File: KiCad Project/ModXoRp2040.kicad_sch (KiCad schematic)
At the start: 0 parts

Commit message: start pcb layout
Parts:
- added J1: LPC, symbol Connector_Generic:Conn_02x08_Odd_Even
- added R1, R2: 100, symbol Device:R_Small
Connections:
- new net: J1.15 (Pin_15), R2.2
- new net: J1.9 (Pin_9), R1.2
- new net 3.3v: R1.1, R2.1
- new net 5v: J1.6 (Pin_6)
- new net GND: J1.12 (Pin_12), J1.2 (Pin_2)
- new net RST: J1.5 (Pin_5)
- no-connect marks 0 -> 2

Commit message: finish schematics, start on pcb layout
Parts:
- added C1, C10, C11, C12, C13, C14, C17, C18, C2, C20, C4, C6, C7, C8, C9: 100nF, Capacitor_SMD:C_0402_1005Metric, symbol Device:C
- added C15, C16: 10uF, Capacitor_SMD:C_0805_2012Metric, symbol Device:C
- added C19, C3, C5: 1uF, Capacitor_SMD:C_0402_1005Metric, symbol Device:C
- added CXTAL1, CXTAL2: 30pF, Capacitor_SMD:C_0402_1005Metric, symbol Device:C_Small
- added D1: D_Schottky, Diode_SMD:D_SMA, symbol Device:D_Schottky
- added D3: WS2812B, LED_SMD:LED_WS2812B_PLCC4_5.0x5.0mm_P3.2mm, symbol LED:WS2812B
- added D4: STM_LED2, LED_SMD:LED_0402_1005Metric_Pad0.77x0.64mm_HandSolder, symbol Device:LED
- added D5: SS34, Diode_SMD:D_SMA, symbol Device:D_Schottky
- added FU1: 0.5A, Fuse:Fuse_1206_3216Metric_Pad1.42x1.75mm_HandSolder, symbol Device:Fuse
- added J10: STM EN SCL, Jumper:SolderJumper-2_P1.3mm_Open_RoundedPad1.0x1.5mm, symbol Connector_Generic:Conn_01x02
- added J11: USB_C_Receptacle_USB2.0, Connector_USB:USB_C_Receptacle_G-Switch_GT-USB-7010ASV, symbol Connector:USB_C_Receptacle_USB2.0
- added J12: Conn_01x05, Connector_PinSocket_2.54mm:PinSocket_1x05_P2.54mm_Vertical, symbol Connector_Generic:Conn_01x05
- added J13: Display Exp, Connector_JST:JST_SH_SM06B-SRSS-TB_1x06-1MP_P1.00mm_Horizontal, symbol Connector_Generic:Conn_01x06
- added J2: PROG SM32, Connector_PinSocket_2.54mm:PinSocket_1x08_P2.54mm_Vertical, symbol Connector_Generic:Conn_01x08
- added J3: STM EN, Jumper:SolderJumper-2_P1.3mm_Open_RoundedPad1.0x1.5mm, symbol Connector_Generic:Conn_01x02
- added J4: RGB Exp, Connector_JST:JST_SH_SM06B-SRSS-TB_1x06-1MP_P1.00mm_Horizontal, symbol Connector_Generic:Conn_01x06
- added J5: I2C Exp, Connector_JST:JST_SH_SM06B-SRSS-TB_1x06-1MP_P1.00mm_Horizontal, symbol Connector_Generic:Conn_01x06
- added J6: STM Dbg, Connector_JST:JST_SH_SM06B-SRSS-TB_1x06-1MP_P1.00mm_Horizontal, symbol Connector_Generic:Conn_01x06
- added J8: D0, TestPoint:TestPoint_Pad_D1.5mm, symbol Connector_Generic:Conn_01x01
- added J9: STM EN SDA, Jumper:SolderJumper-2_P1.3mm_Open_RoundedPad1.0x1.5mm, symbol Connector_Generic:Conn_01x02
- added R10, RRST1: 10K, Resistor_SMD:R_0603_1608Metric_Pad0.98x0.95mm_HandSolder, symbol Device:R
- added R11, R9: 1K, Resistor_SMD:R_0402_1005Metric_Pad0.72x0.64mm_HandSolder, symbol Device:R
- added R12, R6: 5.1k, Resistor_SMD:R_0603_1608Metric_Pad0.98x0.95mm_HandSolder, symbol Device:R
- added R13, R14, R15, R5: 2k, Resistor_SMD:R_0402_1005Metric_Pad0.72x0.64mm_HandSolder, symbol Device:R_Small
- added R16: 1K, Resistor_SMD:R_0603_1608Metric_Pad0.98x0.95mm_HandSolder, symbol Device:R
- added R3, R4: 100, Resistor_SMD:R_0402_1005Metric_Pad0.72x0.64mm_HandSolder, symbol Device:R_Small
- added R7, R8: 27, Resistor_SMD:R_0402_1005Metric_Pad0.72x0.64mm_HandSolder, symbol Device:R
- added SWBOOT1, SWRST1: K2-1187SQ-C4SW-06, Jumper:SolderJumper-2_P1.3mm_Open_RoundedPad1.0x1.5mm, symbol Switch:SW_Push
- added U1: RP2040, Package_DFN_QFN:QFN-56-1EP_7x7mm_P0.4mm_EP3.2x3.2mm, symbol MCU_RaspberryPi_RP2040:RP2040
- added U2: USBLC6-2P6, Package_TO_SOT_SMD:SOT-666, symbol Power_Protection:USBLC6-2P6
- added U3: STM32F030C8Tx, Package_QFP:LQFP-48_7x7mm_P0.5mm, symbol MCU_ST_STM32F0:STM32F030C8Tx
- added UF1: W25Q128JVS, libs:SOIC-8_5.275x5.275mm_P1.27mm, symbol Memory_Flash:W25Q128JVS
- added UV1: NCP1117-3.3_SOT223, Package_TO_SOT_SMD:SOT-223-3_TabPin2, symbol Regulator_Linear:NCP1117-3.3_SOT223
- added Y1: 12MHz, Crystal:Crystal_SMD_3225-4Pin_3.2x2.5mm, symbol Device:Crystal_GND24
- J1: footprint (none) -> Connector_PinSocket_2.54mm:PinSocket_2x08_P2.54mm_Vertical
- R1, R2: footprint (none) -> Resistor_SMD:R_0402_1005Metric_Pad0.72x0.64mm_HandSolder
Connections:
- net GND: now also C1.2, C10.2, C11.2, C12.1, C13.2, C14.2, C15.2, C16.2, C17.2, C18.2, C19.2, C2.2, C20.2, C3.2, C4.2, C5.2, C6.2, C7.2, C8.2, C9.2, CXTAL1.1, CXTAL2.1, D3.3 (VSS), J11.A1 (GND), J11.A12 (GND), J11.B1 (GND), J11.B12 (GND), J11.S1 (SHIELD), J12.1 (Pin_1), J2.7 (Pin_7), J4.3 (Pin_3), J4.4 (Pin_4), J4.5 (Pin_5), J5.1 (Pin_1), J6.1 (Pin_1), R12.1, R14.2, R16.1, R6.1, SWBOOT1.1, SWRST1.2, U1.19 (TESTEN), U1.57 (GND), U2.2 (GND), U3.23 (VSS), U3.8 (VSSA), UF1.4 (GND), UV1.1 (GND), Y1.2, Y1.4
- net RST: now also U1.9 (GPIO7)
- net LCLK: now reaches J1.1 (Pin_1)
- net LCLK: now also U1.6 (GPIO4)
- net at J1.10 (Pin_10): now also R3.2
- net at J1.11 (Pin_11): now also R2.2
- net XSCL: now reaches J1.13 (Pin_13)
- net XSCL: now also J10.2 (Pin_2), J5.2 (Pin_2)
- net XSDA: now reaches J1.14 (Pin_14)
- net XSDA: now also J5.5 (Pin_5), J9.2 (Pin_2)
- net 3.3v_xb: now reaches J1.15 (Pin_15)
- net 3.3v_xb: now also J1.9 (Pin_9), J4.2 (Pin_2), U1.11 (GPIO8); no longer R2.2
- net LFRAME: now reaches J1.3 (Pin_3)
- net LFRAME: now also U1.7 (GPIO5)
- net at J1.7 (Pin_7): now also R1.2
- net at J1.8 (Pin_8): now also R4.2
- net 3.3v renamed LAD0
- net LAD0: now also U1.2 (GPIO0); no longer R1.1
- net 5v: no longer names the net of J1.6 (Pin_6)
- net 5v: now also D1.2 (A)
- new net: CXTAL2.2, R11.2, Y1.3
- new net: J11.B5 (CC2), R12.2
- new net: J11.A6 (D+), J11.B6 (D+), U2.1 (I/O1)
- new net: J11.A7 (D-), J11.B7 (D-), U2.3 (I/O2)
- new net: FU1.2, J11.A4 (VBUS), J11.A9 (VBUS), J11.B4 (VBUS), J11.B9 (VBUS)
- new net: J11.A5 (CC1), R6.2
- new net: D4.1 (K), R16.2
- new net: D5.2 (A), FU1.1
- new net: R14.1, U3.44 (BOOT0)
- new net +1V1: C1.1, C2.1, C3.1, U1.23 (DVDD), U1.45 (VREG_VOUT), U1.50 (DVDD)
- new net +3V3: C10.1, C11.1, C13.1, C14.1, C16.1, C4.1, C5.1, C6.1, C7.1, C8.1, C9.1, J2.8 (Pin_8), J3.2 (Pin_2), R10.1, R13.1, R15.1, R5.2, RRST1.2, U1.1 (IOVDD), U1.10 (IOVDD), U1.22 (IOVDD), U1.33 (IOVDD), U1.42 (IOVDD), U1.43 (ADC_AVDD), U1.44 (VREG_IN), U1.48 (USB_VDD), U1.49 (IOVDD), UF1.8 (VCC), UV1.2 (VO)
- new net +5V: C15.1, C20.1, D1.1 (K), D3.1 (VDD), D5.1 (K), J13.1 (Pin_1), J4.6 (Pin_6), J5.6 (Pin_6), UV1.3 (VI)
- new net 5V: C12.2, U2.5 (VBUS)
- new net D0: J8.1 (Pin_1), U1.8 (GPIO6)
- new net DISP_CSN1: J13.5 (Pin_5), U1.39 (GPIO27_ADC1)
- new net DISP_CSN2: J13.4 (Pin_4), U1.38 (GPIO26_ADC0)
- new net DISP_SPI_SCK: J13.3 (Pin_3), U1.29 (GPIO18)
- new net DISP_SPI_TX: J13.2 (Pin_2), U1.30 (GPIO19)
- new net EX_SCL: J5.4 (Pin_4), U1.32 (GPIO21)
- new net EX_SDA: J5.3 (Pin_3), U1.31 (GPIO20)
- new net LAD1: R3.1, U1.3 (GPIO1)
- new net LAD2: R4.1, U1.4 (GPIO2)
- new net LAD3: R1.1, U1.5 (GPIO3)
- new net QSPI_SCLK: U1.52 (QSPI_SCLK), UF1.6 (CLK)
- new net QSPI_SD0: U1.53 (QSPI_SD0), UF1.5 (DI(IO0))
- new net QSPI_SD1: U1.55 (QSPI_SD1), UF1.2 (DO(IO1))
- new net QSPI_SD2: U1.54 (QSPI_SD2), UF1.3 (IO2)
- new net QSPI_SD3: U1.51 (QSPI_SD3), UF1.7 (IO3)
- new net QSPI_SS: R10.2, R9.1, U1.56 (QSPI_SS), UF1.1 (~{CS})
- new net RGB: D3.2 (DOUT), J4.1 (Pin_1)
- new net RP2040_RGB: D3.4 (DIN), U1.34 (GPIO22)
- new net RUN: RRST1.1, SWRST1.1, U1.26 (RUN)
- new net STM_3.3v: C17.1, C18.1, C19.1, J3.1 (Pin_1), U3.1 (VDD), U3.24 (VDD), U3.48 (VDD), U3.9 (VDDA)
- new net STM_INT: J6.6 (Pin_6), U3.36 (PF7)
- new net STM_LED: J6.2 (Pin_2), U3.2 (PC13)
- new net STM_LED2: D4.2 (A), U3.3 (PC14)
- new net STM_NRST: J2.3 (Pin_3), R15.2, U3.7 (NRST)
- new net STM_OSC: J2.4 (Pin_4), U3.6 (PF1)
- new net STM_RX: J2.6 (Pin_6), U3.13 (PA3)
- new net STM_SCL: J6.3 (Pin_3), J6.4 (Pin_4), R5.1, U3.42 (PB6)
- new net STM_SDA: J6.5 (Pin_5), R13.2, U3.43 (PB7)
- new net STM_SWCLK: J2.1 (Pin_1), U3.37 (PA14)
- new net STM_SWDIO: J2.2 (Pin_2), U3.34 (PA13)
- new net STM_TX: J2.5 (Pin_5), U3.12 (PA2)
- new net STM_XSCL: J10.1 (Pin_1), U3.21 (PB10)
- new net STM_XSDA: J9.1 (Pin_1), U3.22 (PB11)
- new net SWCLK: J12.3 (Pin_3), U1.24 (SWCLK)
- new net SWDIO: J12.2 (Pin_2), U1.25 (SWD)
- new net UART_RX: J12.4 (Pin_4), U1.28 (GPIO17)
- new net UART_TX: J12.5 (Pin_5), U1.27 (GPIO16)
- new net USB_D+: R7.1, U2.6 (I/O1)
- new net USB_D-: R8.1, U2.4 (I/O2)
- new net USB_M+: R7.2, U1.47 (USB_DP)
- new net USB_M-: R8.2, U1.46 (USB_DM)
- new net XIN: CXTAL1.2, U1.20 (XIN), Y1.1
- new net XOUT: R11.1, U1.21 (XOUT)
- new net ~{USB_BOOT}: R9.2, SWBOOT1.2
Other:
- note added: "12MHz, 20pF"
- note added: "30pF/2 + stray capacitance of 5pF = 20pF"
- note added: "Code Storage"
- note added: "Crystal"
- note added: "Debug Header"
- note added: "Make sure this is close to pin 44 of RP2040"
- note added: "Make sure this is close to pin 45 of RP2040"
- note added: "Power Delivery"
- note added: "RGB LED"
- note added: "RP2040 Circuitry"
- note added: "Run SW"
- note added: "STM32 Circuitry"
- note added: "USB/PD Circuitry"
- moved on the sheet: J1, R1, R2

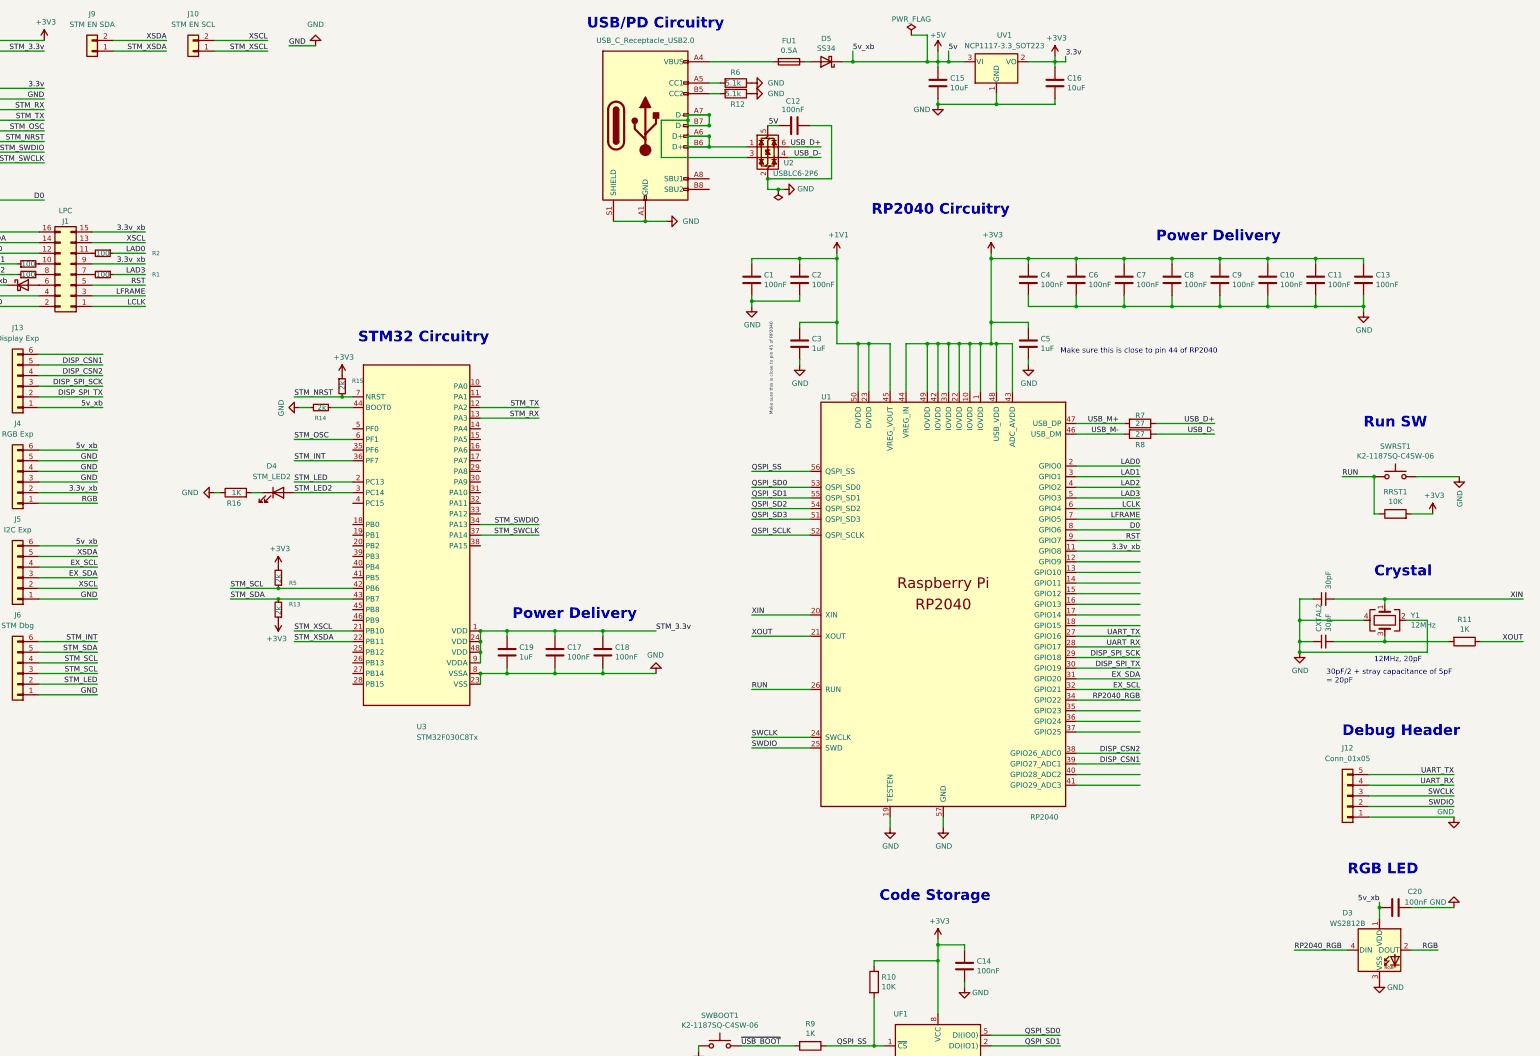
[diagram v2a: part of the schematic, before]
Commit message: continue layout, put some tracks down
need to rotate rp2040 otherwise layout is pretty much final?
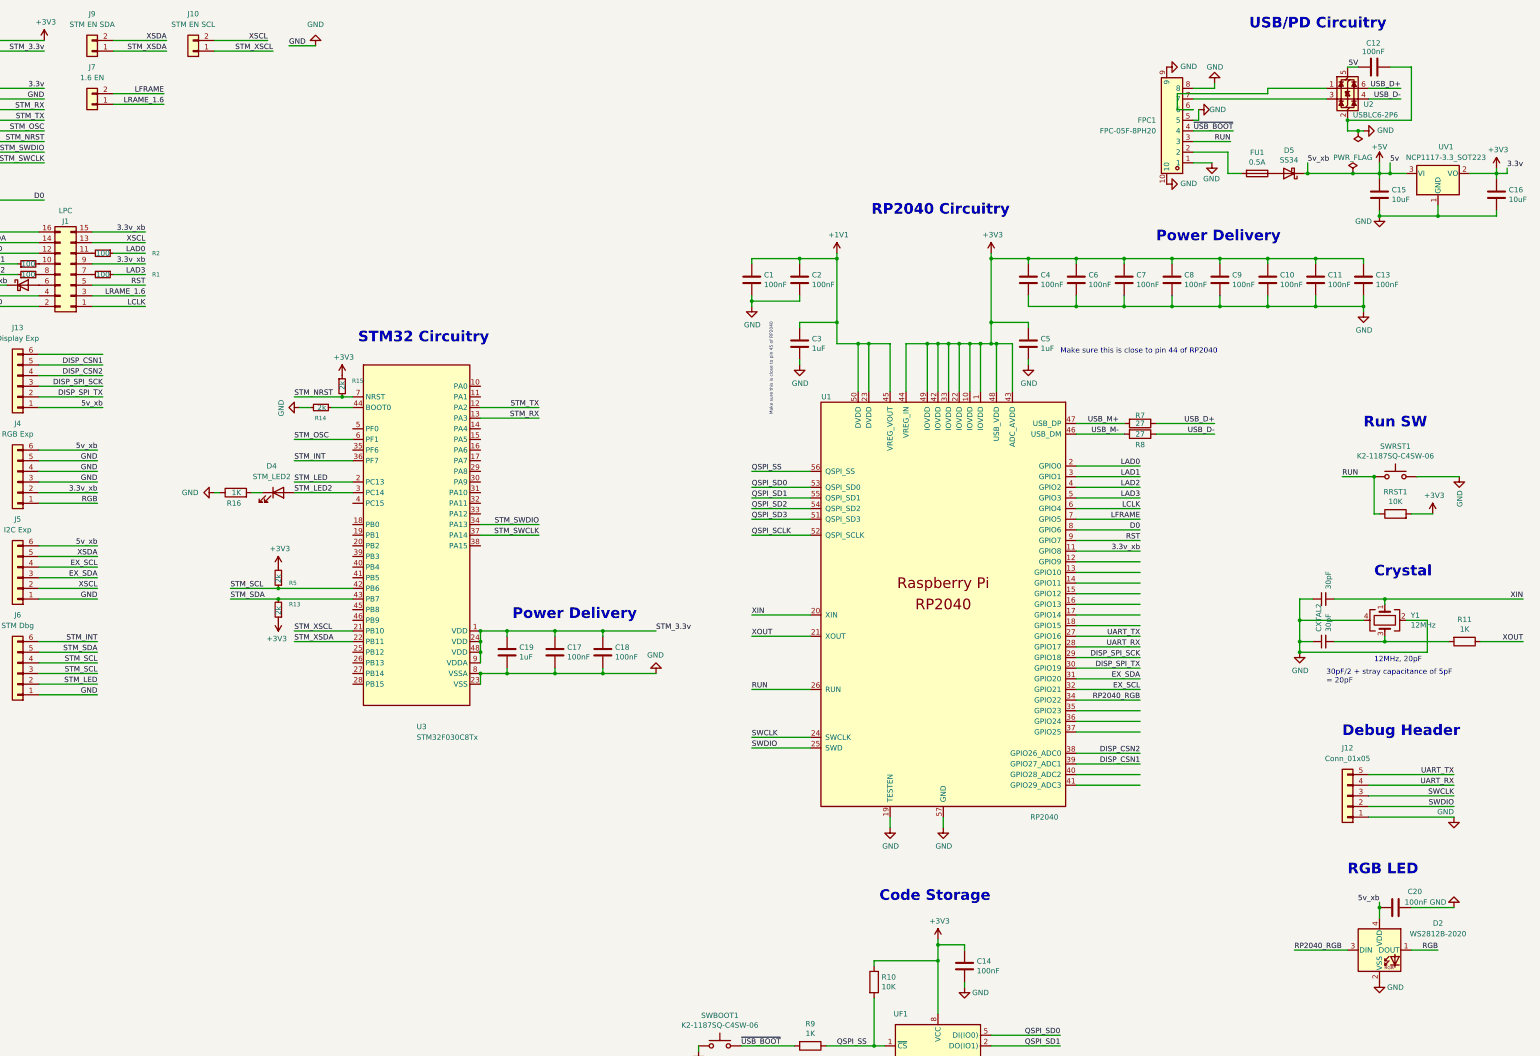
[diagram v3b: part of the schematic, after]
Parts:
- removed D3: WS2812B, LED_SMD:LED_WS2812B_PLCC4_5.0x5.0mm_P3.2mm, symbol LED:WS2812B
- removed J11: USB_C_Receptacle_USB2.0, Connector_USB:USB_C_Receptacle_G-Switch_GT-USB-7010ASV, symbol Connector:USB_C_Receptacle_USB2.0
- removed R12, R6: 5.1k, Resistor_SMD:R_0603_1608Metric_Pad0.98x0.95mm_HandSolder, symbol Device:R
- added D2: WS2812B-2020, LED_SMD:LED_WS2812B-2020_PLCC4_2.0x2.0mm, symbol LED:WS2812B-2020
- added FPC1: FPC-05F-8PH20, fpc:FPC-SMD_8P-P0.50_FPC-05F-8PH20, symbol libs:FPC-05F-8PH20
- added J7: 1.6 EN, Jumper:SolderJumper-2_P1.3mm_Open_RoundedPad1.0x1.5mm, symbol Connector_Generic:Conn_01x02
- C1, C10, C11, C12, C13, C14, C17, C18, C19, C2, C20, C3, C4, C5, C6, C7, C8, C9, CXTAL1, CXTAL2: footprint Capacitor_SMD:C_0402_1005Metric -> Capacitor_SMD:C_0201_0603Metric
- C15, C16: footprint Capacitor_SMD:C_0805_2012Metric -> Capacitor_SMD:C_0201_0603Metric
- J12: footprint Connector_PinSocket_2.54mm:PinSocket_1x05_P2.54mm_Vertical -> Connector_PinSocket_2.00mm:PinSocket_1x05_P2.00mm_Vertical
- R1, R11, R13, R14, R15, R2, R3, R4, R5, R7, R8, R9: footprint Resistor_SMD:R_0402_1005Metric_Pad0.72x0.64mm_HandSolder -> Resistor_SMD:R_0201_0603Metric
- R10, R16, RRST1: footprint Resistor_SMD:R_0603_1608Metric_Pad0.98x0.95mm_HandSolder -> Resistor_SMD:R_0402_1005Metric
- UF1: footprint libs:SOIC-8_5.275x5.275mm_P1.27mm -> fpc:SOIC-8_5.275x5.275mm_P1.27mm
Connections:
- net +5V: now also D2.4 (VDD)
- net GND: now also D2.2 (VSS), FPC1.1, FPC1.10, FPC1.5, FPC1.8, FPC1.9
- net LFRAME: now also J7.2 (Pin_2); no longer J1.3 (Pin_3)
- net RGB: now also D2.1 (DOUT)
- net RP2040_RGB: now also D2.3 (DIN)
- net RUN: now also FPC1.3
- net ~{USB_BOOT}: now also FPC1.4
- net at U2.1 (I/O1): now also FPC1.6
- net at U2.3 (I/O2): now also FPC1.7
- net at FU1.2: now also FPC1.2
- new net LRAME_1.6: J1.3 (Pin_3), J7.1 (Pin_1)
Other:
- moved on the sheet: C12, C15, C16, D5, FU1, U2, UV1

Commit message: semi update
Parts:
- removed J7: 1.6 EN, Jumper:SolderJumper-2_P1.3mm_Open_RoundedPad1.0x1.5mm, symbol Connector_Generic:Conn_01x02
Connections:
- net LRAME_1.6 is gone; now on net LFRAME: J1.3 (Pin_3)
- net GND: now also J13.6 (Pin_6)
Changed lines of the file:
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@@
 	(wire
 		(pts
-			(xy 62.23 35.56) (xy 74.295 35.56)
-		)
-		(stroke
-			(width 0)
-			(type default)
-		)
-	)
-	(wire
-		(pts
 			(xy 292.1 195.58) (xy 307.34 195.58)
 		)
@@
 	(wire
 		(pts
-			(xy 62.23 33.02) (xy 74.295 33.02)
-		)
-		(stroke
-			(width 0)
-			(type default)
-		)
-	)
-	(wire
-		(pts
 			(xy 265.43 237.49) (xy 265.43 236.22)
 		)
@@
 		)
 	)
-	(label "LFRAME"
-		(at 74.295 33.02 180)
-		(fields_autoplaced yes)
-		(effects
-			(font
-				(size 1.27 1.27)
-			)
-			(justify right bottom)
-		)
-		(property "LFRAME" ""
-			(at 74.295 34.29 0)
-			(effects
-				(font
-					(size 1.27 1.27)
-					(italic yes)
-				)
-				(justify right)
-			)
-		)
-	)
 	(label "SWDIO"
 		(at 382.27 203.2 180)
@@
 		)
 	)
+	(label "LFRAME"
+		(at 69.85 81.28 180)
+		(fields_autoplaced yes)
+		(effects
+			(font
+				(size 1.27 1.27)
+			)
+			(justify right bottom)
+		)
+		(property "LFRAME" ""
+			(at 69.85 82.55 0)
+			(effects
+				(font
+					(size 1.27 1.27)
+					(italic yes)
+				)
+				(justify right)
+			)
+		)
+	)
 	(label "STM_INT"
 		(at 105.41 120.65 0)
@@
 		)
 	)
-	(label "LRAME_1.6"
-		(at 69.85 81.28 180)
-		(fields_autoplaced yes)
-		(effects
-			(font
-				(size 1.27 1.27)
-			)
-			(justify right bottom)
-		)
-		(property "LRAME_1.6" ""
-			(at 69.85 82.55 0)
-			(effects
-				(font
-					(size 1.27 1.27)
-					(italic yes)
-				)
-				(justify right)
-			)
-		)
-	)
 	(label "DISP_SPI_TX"
 		(at 59.69 105.41 180)
@@
 		)
 	)
+	(label "GND"
+		(at 59.69 95.25 180)
+		(fields_autoplaced yes)
+		(effects
+			(font
+				(size 1.27 1.27)
+			)
+			(justify right bottom)
+		)
+		(property "GND" ""
+			(at 59.69 96.52 0)
+			(effects
+				(font
+					(size 1.27 1.27)
+					(italic yes)
+				)
+				(justify right)
+			)
+		)
+	)
 	(label "D0"
 		(at 307.34 137.16 180)
@@
 		)
 	)
-	(label "LRAME_1.6"
-		(at 74.295 35.56 180)
-		(fields_autoplaced yes)
-		(effects
-			(font
-				(size 1.27 1.27)
-			)
-			(justify right bottom)
-		)
-		(property "LRAME_1.6" ""
-			(at 74.295 36.83 0)
-			(effects
-				(font
-					(size 1.27 1.27)
-					(italic yes)
-				)
-				(justify right)
-			)
-		)
-	)
 	(label "GND"
 		(at 31.75 83.82 0)
@@
 					(unit 1)
 				)
-			)
-		)
-	)
-	(symbol
-		(lib_id "Connector_Generic:Conn_01x02")
-		(at 57.15 35.56 180)
-		(unit 1)
-		(exclude_from_sim no)
-		(in_bom yes)
-		(on_board yes)
-		(dnp no)
-		(fields_autoplaced yes)
-		(property "Reference" "J7"
-			(at 57.15 26.67 0)
-			(effects
-				(font
-					(size 1.27 1.27)
-				)
-			)
-		)
-		(property "Value" "1.6 EN"
-			(at 57.15 29.21 0)
-			(effects
-				(font
-					(size 1.27 1.27)
-				)
-			)
-		)
-		(property "Footprint" "Jumper:SolderJumper-2_P1.3mm_Open_RoundedPad1.0x1.5mm"
-			(at 57.15 35.56 0)
-			(effects
-				(font
-					(size 1.27 1.27)
-				)
-				(hide yes)
-			)
-		)
-		(property "Datasheet" "~"
-			(at 57.15 35.56 0)
-			(effects
-				(font
-					(size 1.27 1.27)
-				)
-				(hide yes)
-			)
-		)
-		(property "Description" "Generic connector, single row, 01x02, script generated (kicad-library-utils/schlib/autogen/connector/)"
-			(at 57.15 35.56 0)
-			(effects
-				(font
-					(size 1.27 1.27)
-				)
-				(hide yes)
-			)
-		)
-		(pin "1"
-		)
-		(pin "2"
-		)
-		(instances
-			(project "ModXoRp2040"
-				(path "/b3e3495c-a7b3-4bbf-ac79-be9f84f367cc"
-					(reference "J7")
-					(unit 1)
-				)
